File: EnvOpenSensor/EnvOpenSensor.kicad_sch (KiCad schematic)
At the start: 36 parts, among them J1 HRO_TYPE-C-31-M-12, Q1 BSS138, Q2 BSS138, SW1 SW_Push, SW2 SW_Push, SW3 SW_Push, SW4 SW_Push, U1 Si7021-A20, U2 TPS63001DRCR, U3 SCD41-D-R2

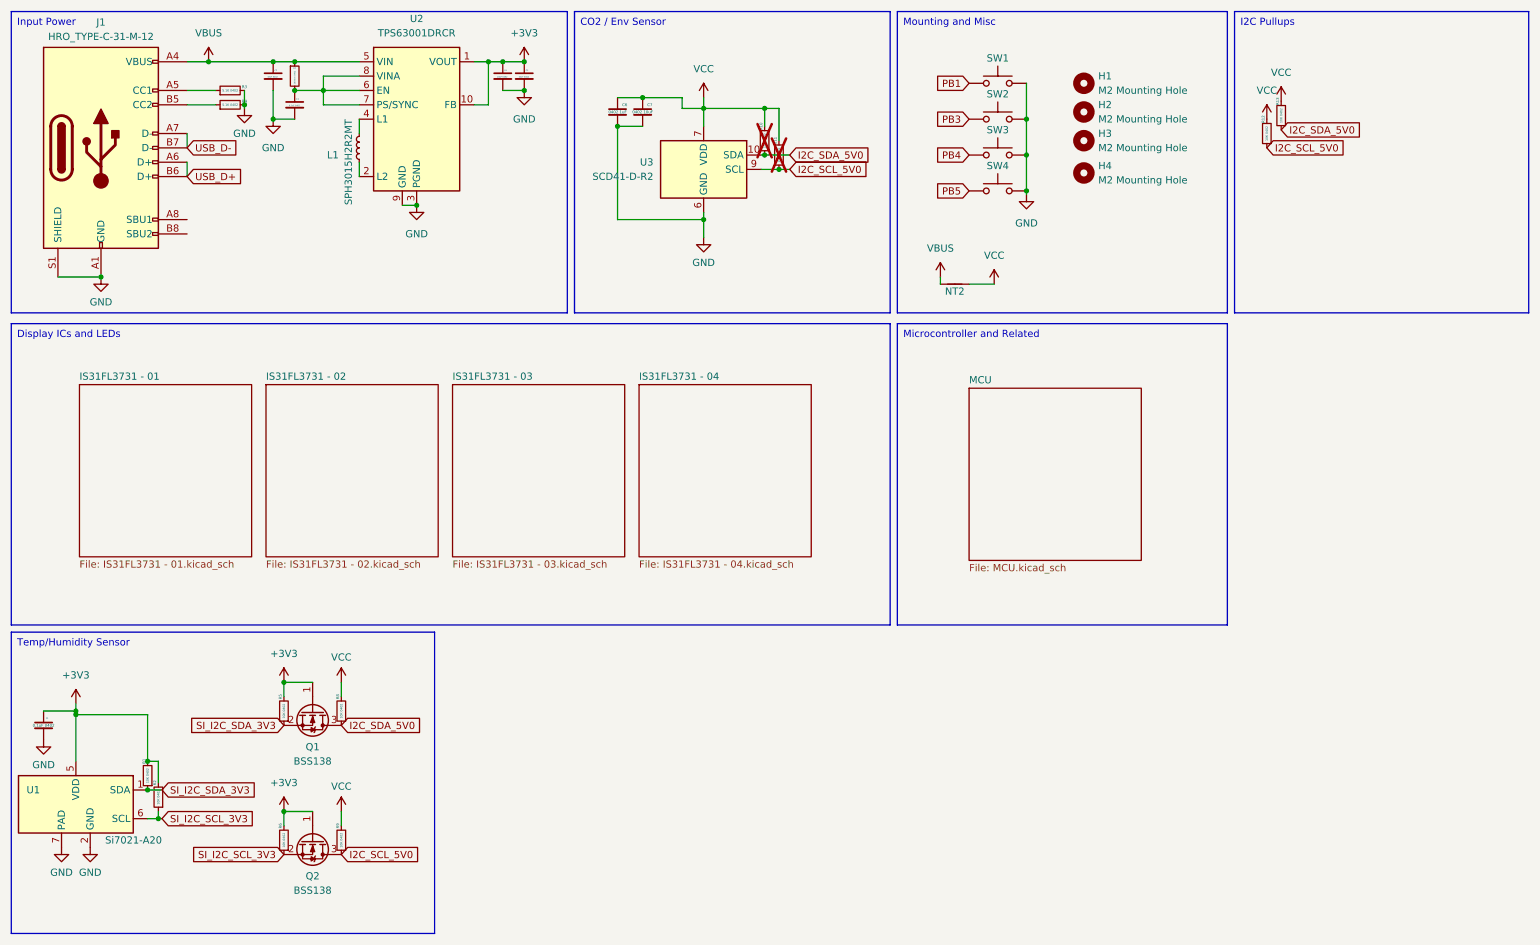
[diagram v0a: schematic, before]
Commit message: Added level shifter IC and fixed incorrect wiring + label
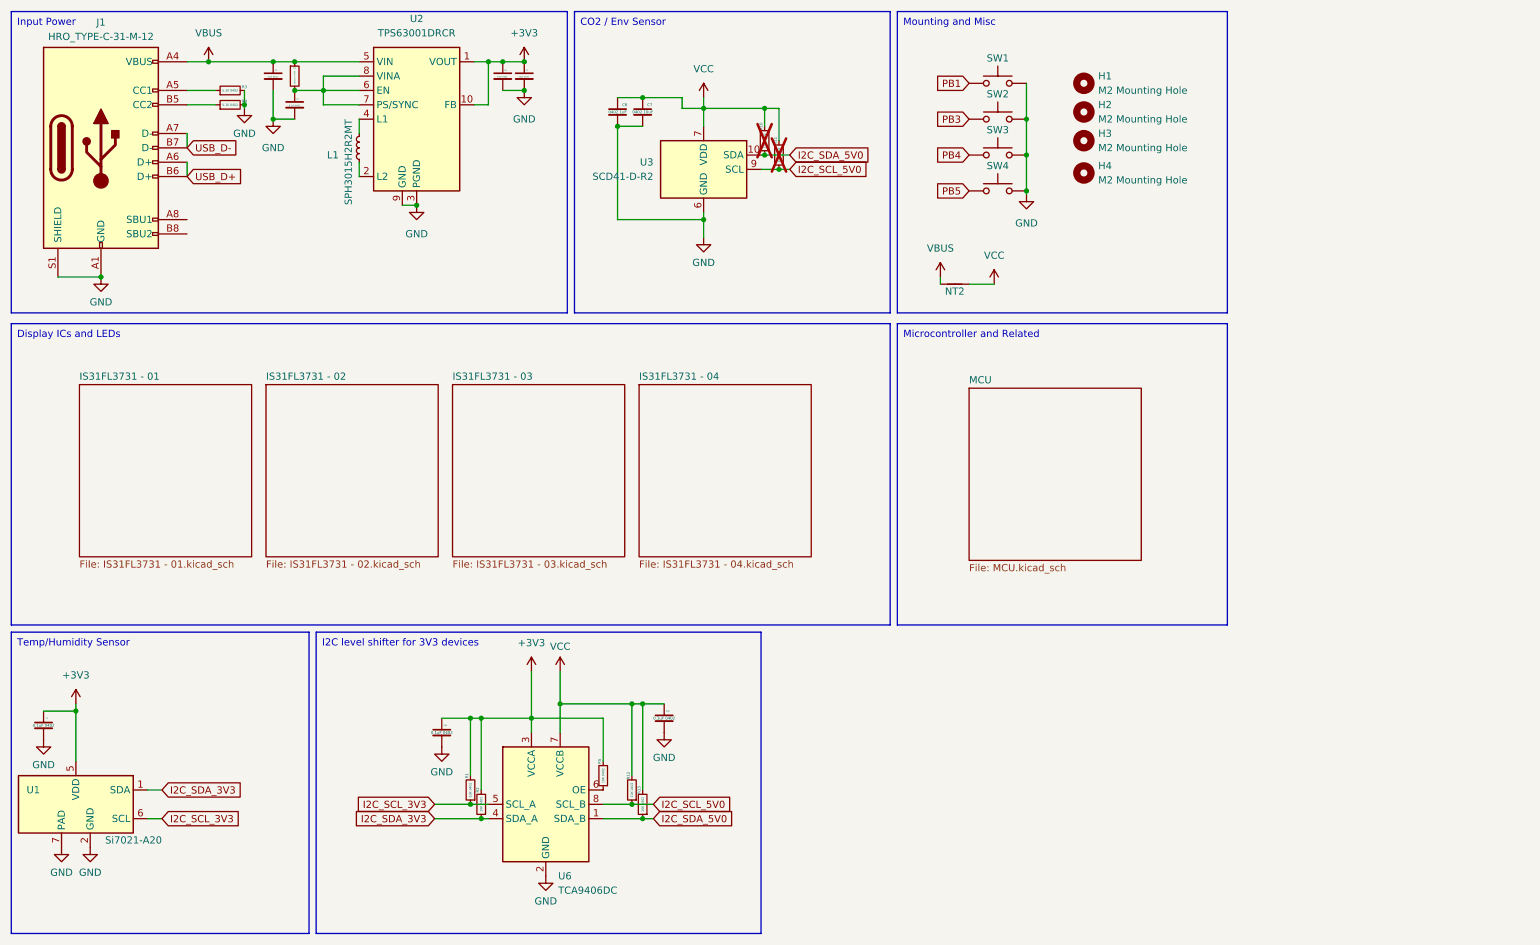
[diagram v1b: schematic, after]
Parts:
- removed Q1, Q2: BSS138, Package_TO_SOT_SMD:SOT-23, symbol Transistor_FET:BSS138
- removed R6, R8, R9: 10K 0402, Resistor_SMD:R_0402_1005Metric, symbol Device:R_Small
- added C45, C46: 0.1uF 0402, Capacitor_SMD:C_0402_1005Metric, symbol Device:C_Small
- added U6: TCA9406DC, Package_SO:VSSOP-8_2.3x2mm_P0.5mm, symbol Interface:TCA9406DC
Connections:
- net +3V3: now also C45.1, U6.3 (VCCA)
- net GND: now also C45.2, C46.2, U6.2 (GND)
- net I2C_SCL_5V0: now also U6.8 (SCL_B)
- net I2C_SDA_5V0: now also U6.1 (SDA_B)
- net VCC: now also C46.1, U6.7 (VCCB)
- net SI_I2C_SCL_3V3 renamed I2C_SCL_3V3
- net I2C_SCL_3V3: now also R1.1, U6.5 (SCL_A); no longer R2.1
- removed net SI_I2C_SDA_3V3: R1.1, R5.1, U1.1 (SDA)
- new net: R5.1, U6.6 (OE)
- new net I2C_SDA_3V3: R2.1, U1.1 (SDA), U6.4 (SDA_A)
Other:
- moved on the sheet: R12, R13
